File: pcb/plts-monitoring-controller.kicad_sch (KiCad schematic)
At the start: 0 parts

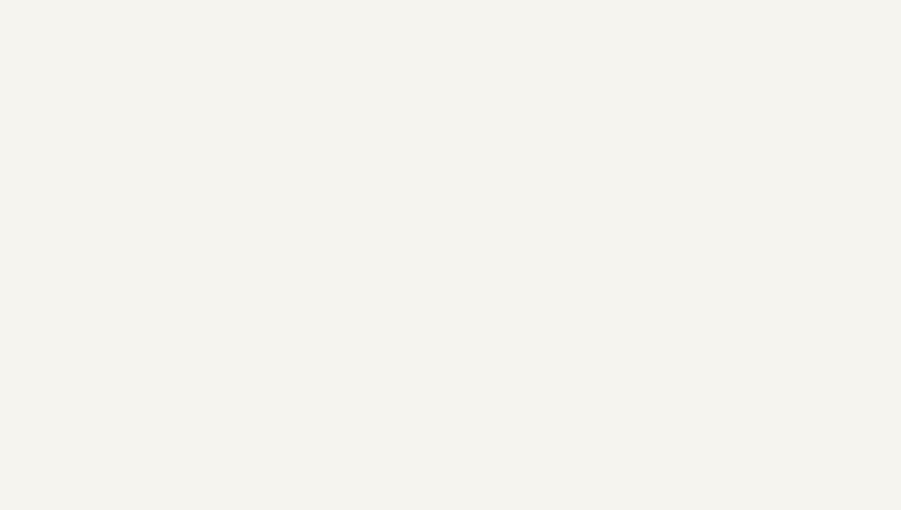
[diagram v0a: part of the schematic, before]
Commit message: pcb: S12 relay-expansion integration + R1/R2 e-stop fixes (schematic + board)
- 09_EMERGENCY: R1 fix (active-LOW drive: R72 high-side from +3V3, OPT1 cathode
  -> RELAY_CTRL, R78 10k pull-up fail-safe) + R2 fix (inverting sense: Q21
  BSS138 + R77 100k divider + R76 revalued 10k pull-up, C75 filter; HIGH=trip
  matches GPIO14 INPUT_PULLUP contract); truth table/docs updated
- NEW 12_RELAY_EXP: F4 1.1A + FB2 -> +5V_RELAY_EXP rail, J_RELAY_EXP 2x03,
  BSS138 I2C shifters Q22/Q23 + R79/R84 4k7, TVS D24/D25 DNP, INT divider
  R82/R83 (PCF8574 module external, 0x20, active-LOW)
- root sch: sheet 12 entry (page 13); plts-custom: +5V_RELAY_EXP symbol
- pro: PWR netclass pattern for +5V_RELAY_EXP
- 01_POWER: C52 22uF->47uF 25V X5R (relay coil dip headroom)
- board: +7 nets, +14 footprints, pad re-netting, placement to 0 structural
  DRC; repaired broken hand-drawn courtyards (M1/U1/K1/J_I2C_EXP) to true
  geometry; U1 antenna keepout respected

ERC: 0 violations (13 sheets). DRC: 0 structural (courtyard/short/keepout/
clearance clean; silk/via/thermal/isolated = post-routing cleanup).
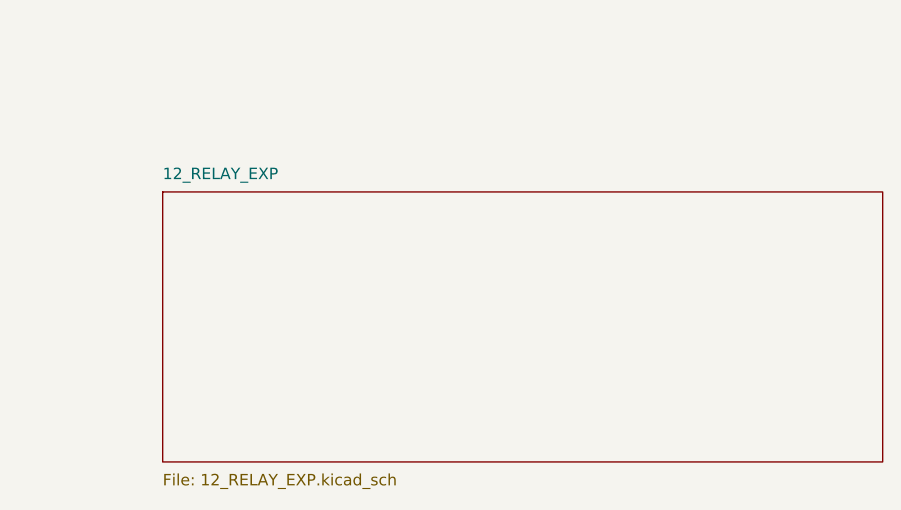
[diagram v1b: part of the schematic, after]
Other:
- added sheet 12_RELAY_EXP (12_RELAY_EXP.kicad_sch)
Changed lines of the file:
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@@
 		(rev "1.0")
 		(company "PLTS Monitoring Project")
-		(comment 1 "Hierarki 12 sheet §45 — S0 skeleton; konten per sheet diisi tahap S1-S11")
+		(comment 1 "Hierarki 13 sheet §45 + S12 relay-exp — S0 skeleton; konten per sheet diisi tahap S1-S11")
 		(comment 2 "Sumber: Brief v1.1 + Audit Report v1.0 + Task Spec v1.0")
 	)
@@
 				)
 			)
+		)
+	)
+	(sheet
+		(at 400 330)
+		(size 80 30)
+		(stroke (width 0.1524) (type solid))
+		(fill (color 0 0 0 0.0000))
+		(property "Sheetname" "12_RELAY_EXP"
+			(at 400 328.73 0)
+			(effects (font (size 1.27 1.27)) (justify left bottom))
+		)
+		(property "Sheetfile" "12_RELAY_EXP.kicad_sch"
+			(at 400 361.27 0)
+			(effects (font (size 1.27 1.27)) (justify left top))
+		)
+		(instances
+			(project "plts-monitoring-controller"
+				(path "/00000000-0000-4000-8000-000000000001"
+					(page "13")
+				)
+			)
